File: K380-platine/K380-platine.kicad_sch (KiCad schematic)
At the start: 38 parts, among them J1 JST-PH 2, J2 Conn_01x23, J3 MicroMod-M.2E, J4 USB_C_Receptacle_USB2.0, J5 Conn_ARM_JTAG_SWD_10, Q1 PMost Enc FET -20V, Q2 Q_NMOS_DGS, SW1 EG1215AA, SW2 SW_Push, SW3 SW_Push, U1 XC6220B331MR, U2 MCP73831-2-OT

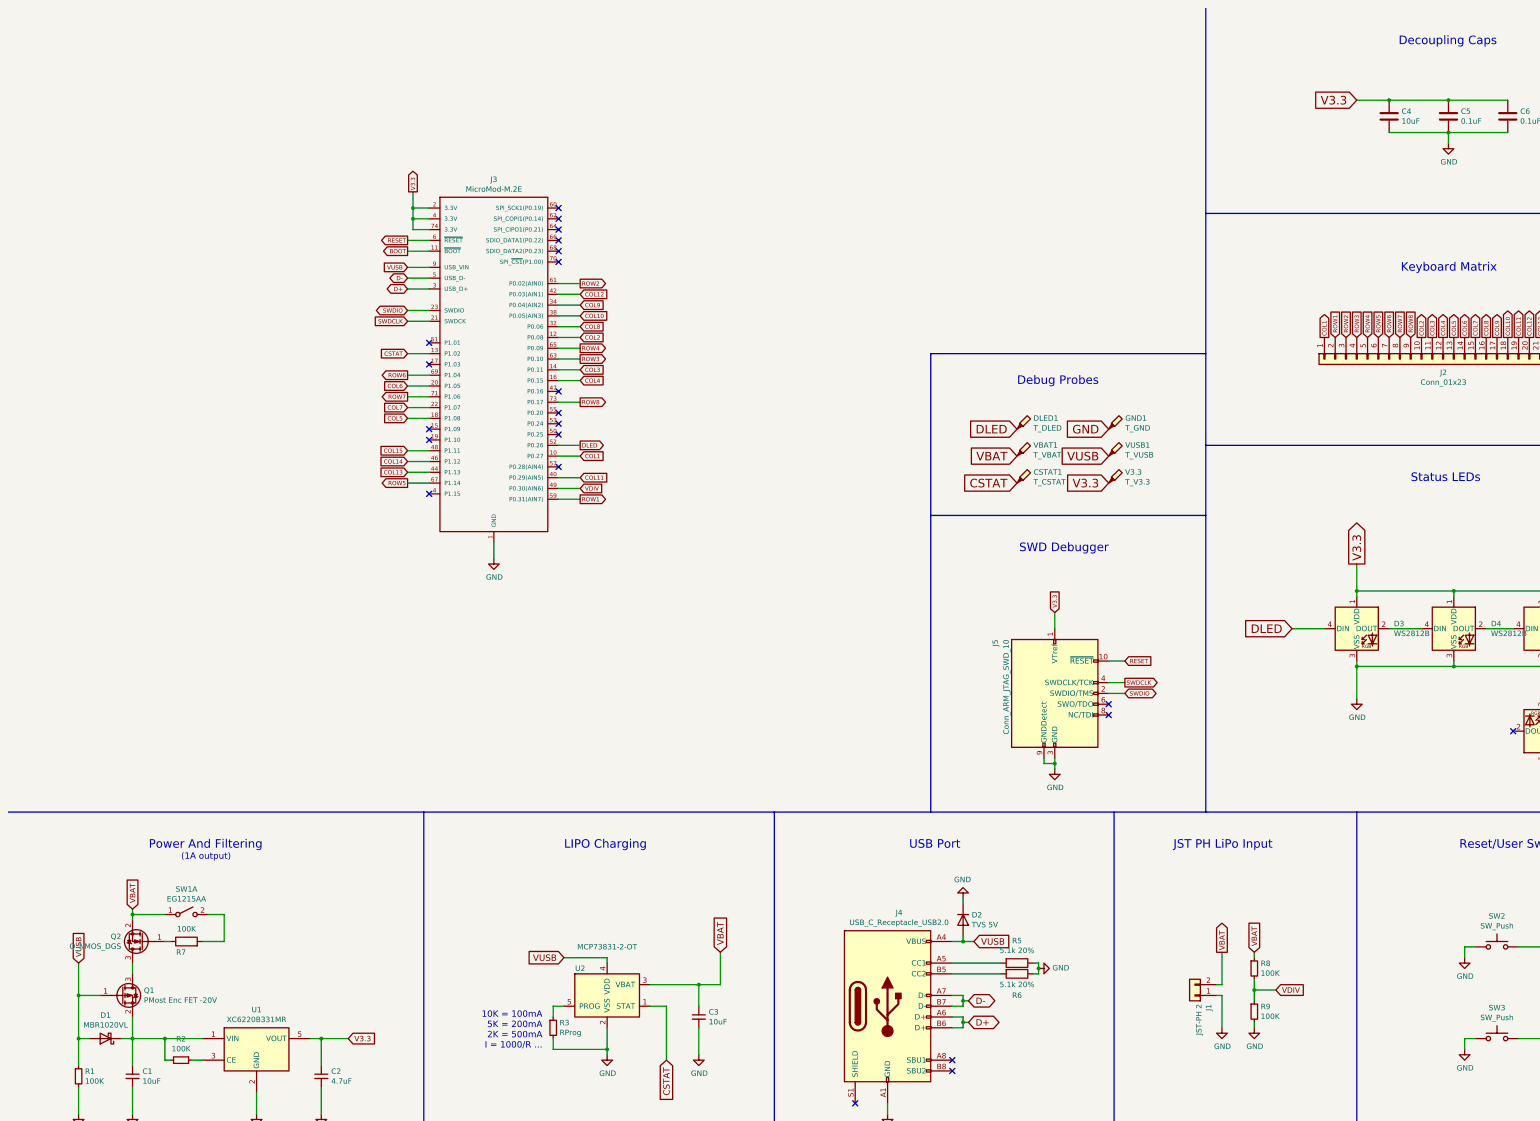
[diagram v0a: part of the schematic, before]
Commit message: keyboard: power: Fixed on/off switch behavior
changes:
- fix on/off switch behavior
- move away from global labels for power symbols
- add SWO trace to Cortex-M debug connector

The on/off switch is a SPDT switch which has two possible
configurations. Use the one where I don't need to invert the signal as
before.

Also fixed up the employed nMOSFET, as it was incorrectly (Drain and
Source was flipped). Also added pull-down resistor to gate.

Signed-off-by: Sophie Friedrich <dev@flowerpot.me>
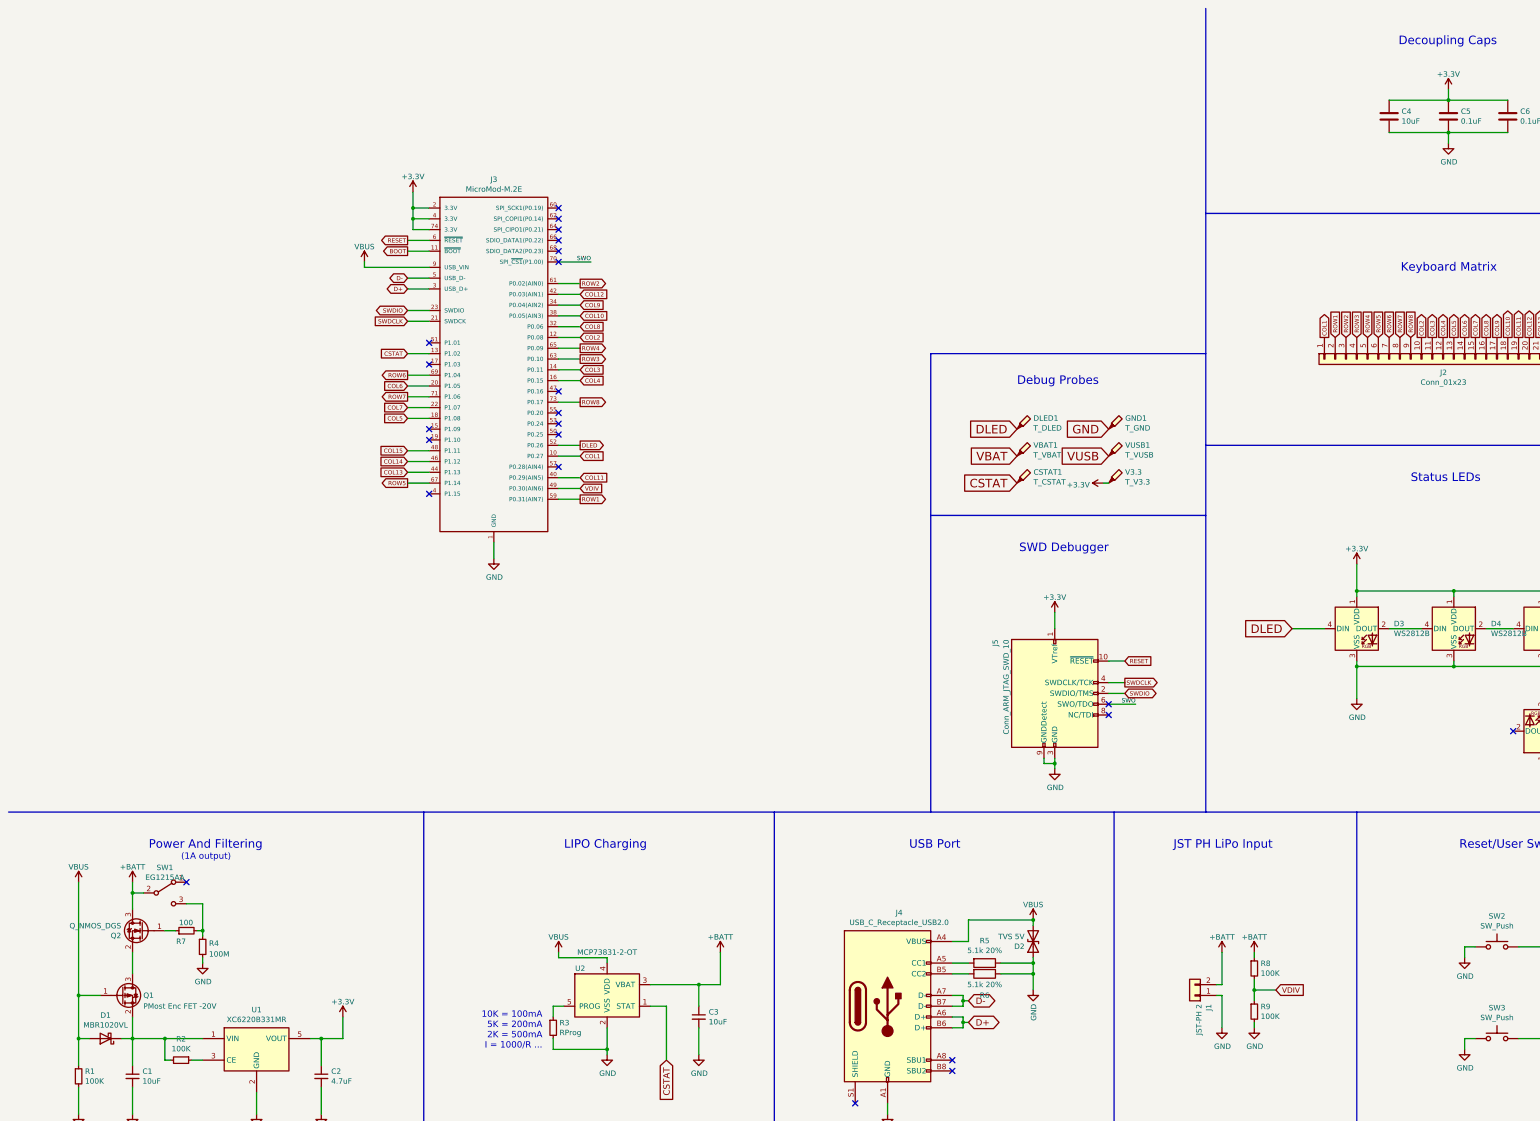
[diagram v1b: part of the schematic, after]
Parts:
- added R4: 100M, Resistor_SMD:R_0603_1608Metric_Pad0.98x0.95mm_HandSolder, symbol Device:R_Small
- D2: symbol Device:D -> Device:D_TVS
- R7: value 100K -> 100; symbol Device:R -> Device:R_Small
- SW1: symbol Switch:SW_DPST_x2 -> Switch:SW_SPDT
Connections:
- net V3.3 is gone; now on net +3V3: C2.1, C4.1, C5.1, C6.1, D3.1 (VDD), D4.1 (VDD), D5.1 (VDD), D6.1 (VDD), J3.2 (3.3V), J3.4 (P1.15), J3.74 (3.3V), J5.1 (VTref), U1.5 (VOUT), V3.3.1
- net GND: now also R4.2
- net VBAT: no longer C3.1, J1.2 (Pin_2), Q2.2 (S), R8.1, SW1.1 (A), U2.3 (VBAT)
- net VUSB: no longer D1.2 (A), D2.2 (A), J3.9 (USB_VIN), J4.A4 (VBUS), J4.A9 (VBUS), J4.B4 (VBUS), J4.B9 (VBUS), Q1.1 (G), R1.1, U2.4 (VDD)
- net at Q1.3 (D): now also Q2.2 (S); no longer Q2.3 (D)
- net +3V3: now reaches J3.4 (P1.15)
- net SWO: now reaches J3.70 (SPI_~{CS1}(P1.00))
- net SWO: now also J5.6 (SWO/TDO)
- net at R7.2: now also SW1.3 (C), R4.1; no longer SW1.2 (B)
- new net +BATT: C3.1, J1.2 (Pin_2), Q2.3 (D), R8.1, SW1.2 (B), U2.3 (VBAT)
- new net VBUS: D1.2 (A), D2.2 (A2), J3.9 (USB_VIN), J4.A4 (VBUS), J4.A9 (VBUS), J4.B4 (VBUS), J4.B9 (VBUS), Q1.1 (G), R1.1, U2.4 (VDD)
- no-connect marks 22 -> 23
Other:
- moved on the sheet: D2, Q2, R5, R6, R7
